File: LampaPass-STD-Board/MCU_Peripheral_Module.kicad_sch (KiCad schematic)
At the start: 0 parts

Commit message: Added draw schematics of MCU and peripheral. Added datasheets of ESP32 dev module and voltage supervisor.
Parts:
- added BZ1: Buzzer, symbol Device:Buzzer
- added C5, C6: 0.1u/6.3V, symbol Device:C_Small
- added C7: 10u/6.3V, symbol Device:C_Small
- added J1, J7: Conn_01x04_Pin, symbol Connector:Conn_01x04_Pin
- added J10: Screw_Terminal_01x05, symbol Connector:Screw_Terminal_01x05
- added J3: Conn_01x02_Pin, symbol Connector:Conn_01x02_Pin
- added J4: Conn_01x08_Socket, symbol Connector:Conn_01x08_Socket
- added J5: Conn_01x03_Socket, symbol Connector:Conn_01x03_Socket
- added J6: Conn_01x06_Pin, symbol Connector:Conn_01x06_Pin
- added J8: Conn_01x04_Socket, symbol Connector:Conn_01x04_Socket
- added Q3, Q4: NMOS, symbol Simulation_SPICE:NMOS
- added R10: 820, symbol Device:R
- added R11, R13, R8, R9: 160, symbol Device:R
- added R12: 1k, symbol Device:R
- added R14, R15, R7: 10k, symbol Device:R
- added U3: ESP32-WROOM-32, RF_Module:ESP32-WROOM-32, symbol RF_Module:ESP32-WROOM-32
- added U5: BD48KxxG, Package_TO_SOT_SMD:SOT-23, symbol Power_Management:BD48KxxG
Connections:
- new net: Q4.2 (G), R13.2
- new net: C5.1, R7.2, U3.3 (EN), U5.2 (VOUT)
- new net: J10.5 (Pin_5), Q4.1 (D)
- new net: BZ1.2 (+), Q3.1 (D), R12.1
- new net: Q3.2 (G), R11.1
- new net: J3.2 (Pin_2), U3.25 (IO0)
- new net +3.3V: BZ1.1 (-), C6.2, C7.2, J1.1 (Pin_1), J10.2 (Pin_2), J4.5 (Pin_5), J5.1 (Pin_1), J6.6 (Pin_6), J7.1 (Pin_1), J8.3 (Pin_3), R12.2, R7.1, U3.2 (VDD), U5.3 (VDD)
- new net +9V: J10.4 (Pin_4)
- new net BLUE: J8.2 (Pin_2), R9.1
- new net BLUE_LED: R9.2, U3.13 (IO14)
- new net BUZZ: R11.2, U3.16 (IO13)
- new net Batt_V_analog: U3.6 (IO34)
- new net Charge_EN: U3.11 (IO26)
- new net Charge_info: U3.10 (IO25)
- new net GND: C5.2, C6.1, C7.1, J1.4 (Pin_4), J3.1 (Pin_1), J4.6 (Pin_6), J5.3 (Pin_3), J6.1 (Pin_1), J7.4 (Pin_4), Q3.3 (S), Q4.3 (S), R14.1, R15.1, U3.1 (GND), U3.15 (GND), U3.38 (GND), U3.39 (GND), U5.1 (GND)
- new net GREEN: J8.1 (Pin_1), R8.1
- new net GREEN_LED: R8.2, U3.14 (IO12)
- new net MISO1: J4.2 (Pin_2), J6.3 (Pin_3), U3.30 (IO18)
- new net MOSI1: J4.3 (Pin_3), J6.4 (Pin_4), U3.31 (IO19)
- new net NC_Solenoid: J10.3 (Pin_3), R14.2, U3.36 (IO22)
- new net NO_Solenoid: J10.1 (Pin_1), R15.2, U3.37 (IO23)
- new net PIR_data: J5.2 (Pin_2), U3.7 (IO35)
- new net RED: J8.4 (Pin_4), R10.1
- new net RED_LED: R10.2, U3.12 (IO27)
- new net SLK1: J4.1 (Pin_1), J6.2 (Pin_2), U3.29 (IO5)
- new net SS_Out_Spi: J6.5 (Pin_5), U3.24 (IO2)
- new net SS_pn532: J4.4 (Pin_4), U3.23 (IO15)
- new net Solenoid: R13.1, U3.26 (IO4)
- new net UART0_ESP32_RX: J1.3 (Pin_3), U3.34 (RXD0/IO3)
- new net UART0_ESP32_TX: J1.2 (Pin_2), U3.35 (TXD0/IO1)
- new net UART2_ESP32_RX: J7.3 (Pin_3), U3.27 (IO16)
- new net UART2_ESP32_TX: J7.2 (Pin_2), U3.28 (IO17)
- no-connect marks 0 -> 8
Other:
- note added: "BOOT OPTION"
- note added: "CONN PIR AM312"
- note added: "CONN pn532"
- note added: "RGB LED CONN"
- note added: "SPI CONN"
- note added: "Solenoid CONN"
- note added: "UART0 DOWNLOAD"
- note added: "UART2 CONN"
- note added: "Worning Can be placed upside down!"

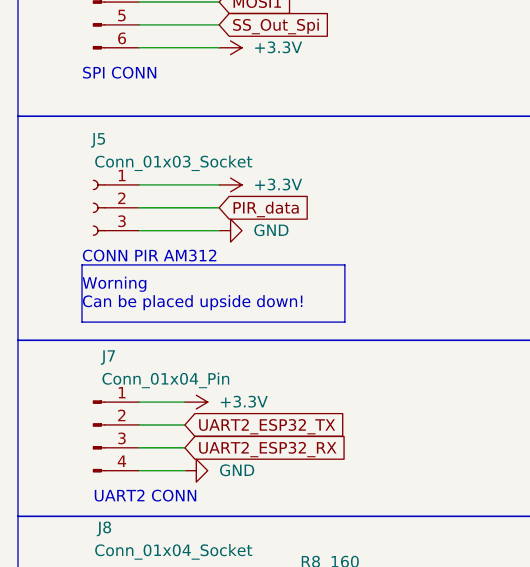
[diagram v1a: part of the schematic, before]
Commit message: Added Battery Backup Power Module. Added Power Mangement empty schematic.
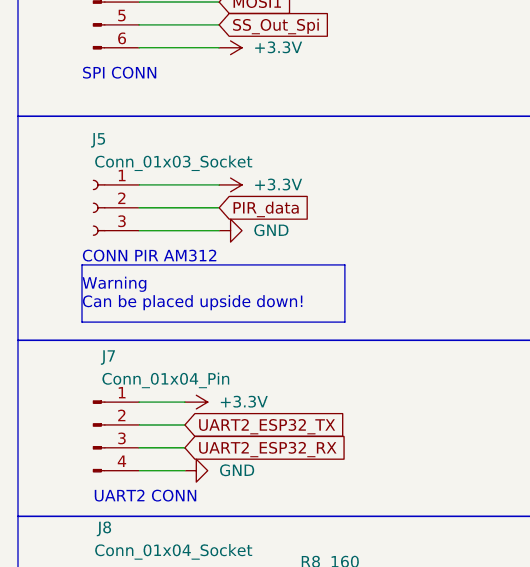
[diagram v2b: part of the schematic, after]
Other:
- note added: "Warning Can be placed upside down!"
- note removed: "Worning Can be placed upside down!"
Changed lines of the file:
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@@
     (effects (font (size 1.27 1.27)) (justify left bottom))
   )
-  (text "Worning \nCan be placed upside down!" (at 19.05 92.71 0)
+  (text "Warning \nCan be placed upside down!" (at 19.05 92.71 0)
     (effects (font (size 1.27 1.27)) (justify left bottom))
   )

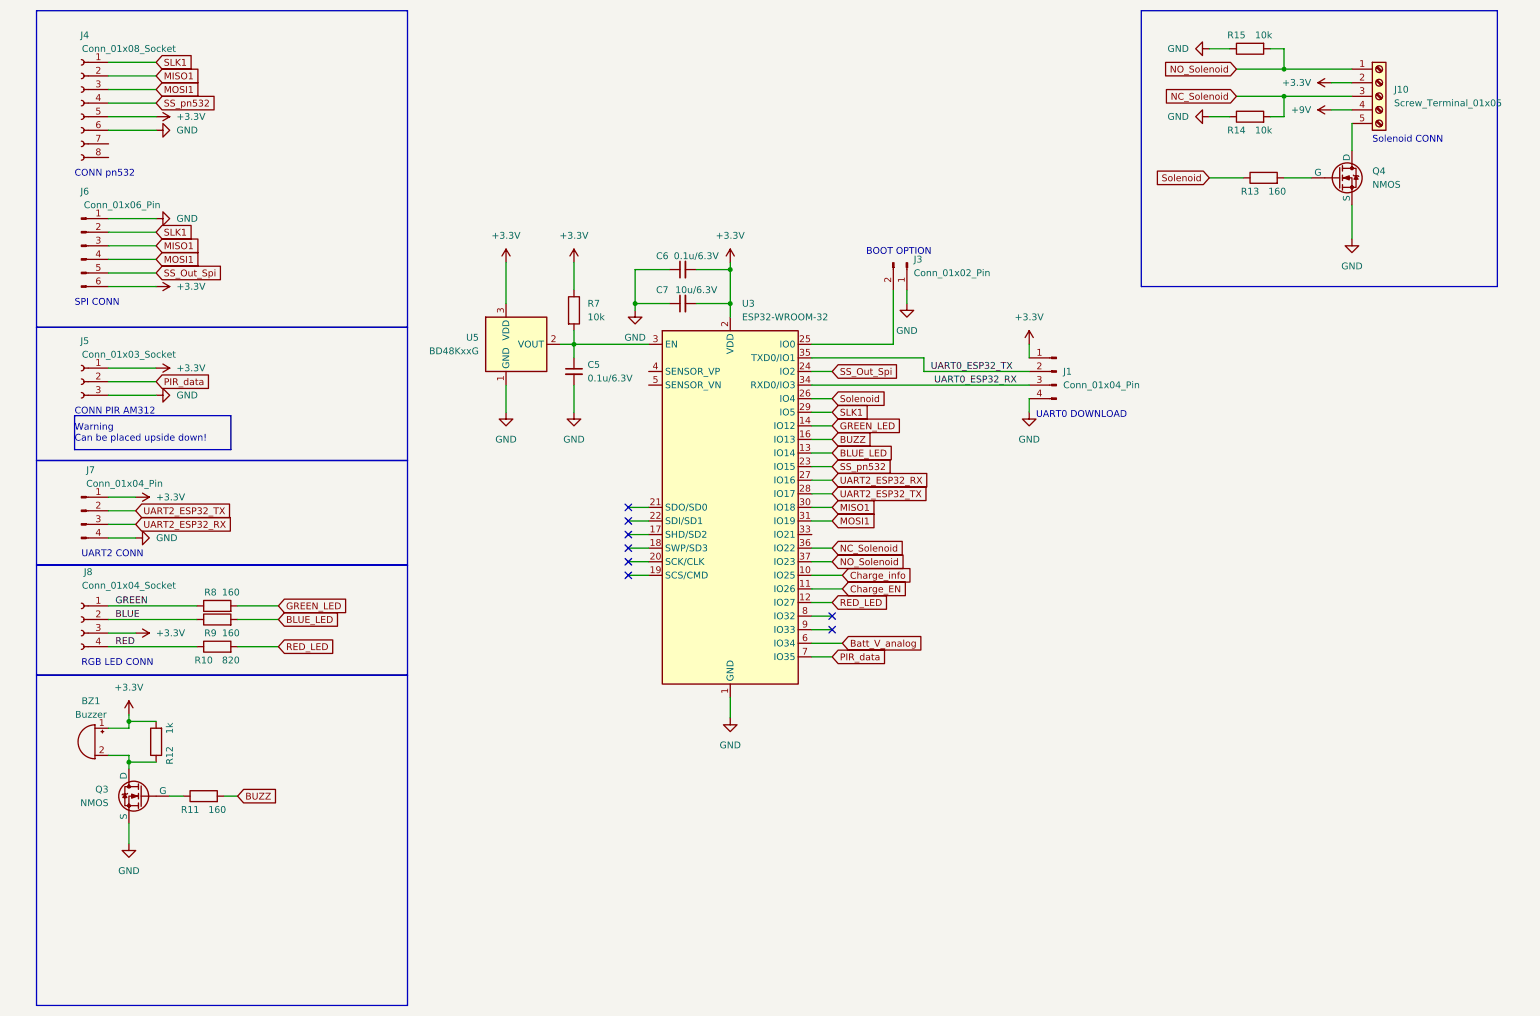
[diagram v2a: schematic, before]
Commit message: Selected connectors and transistors, added footprints for them.
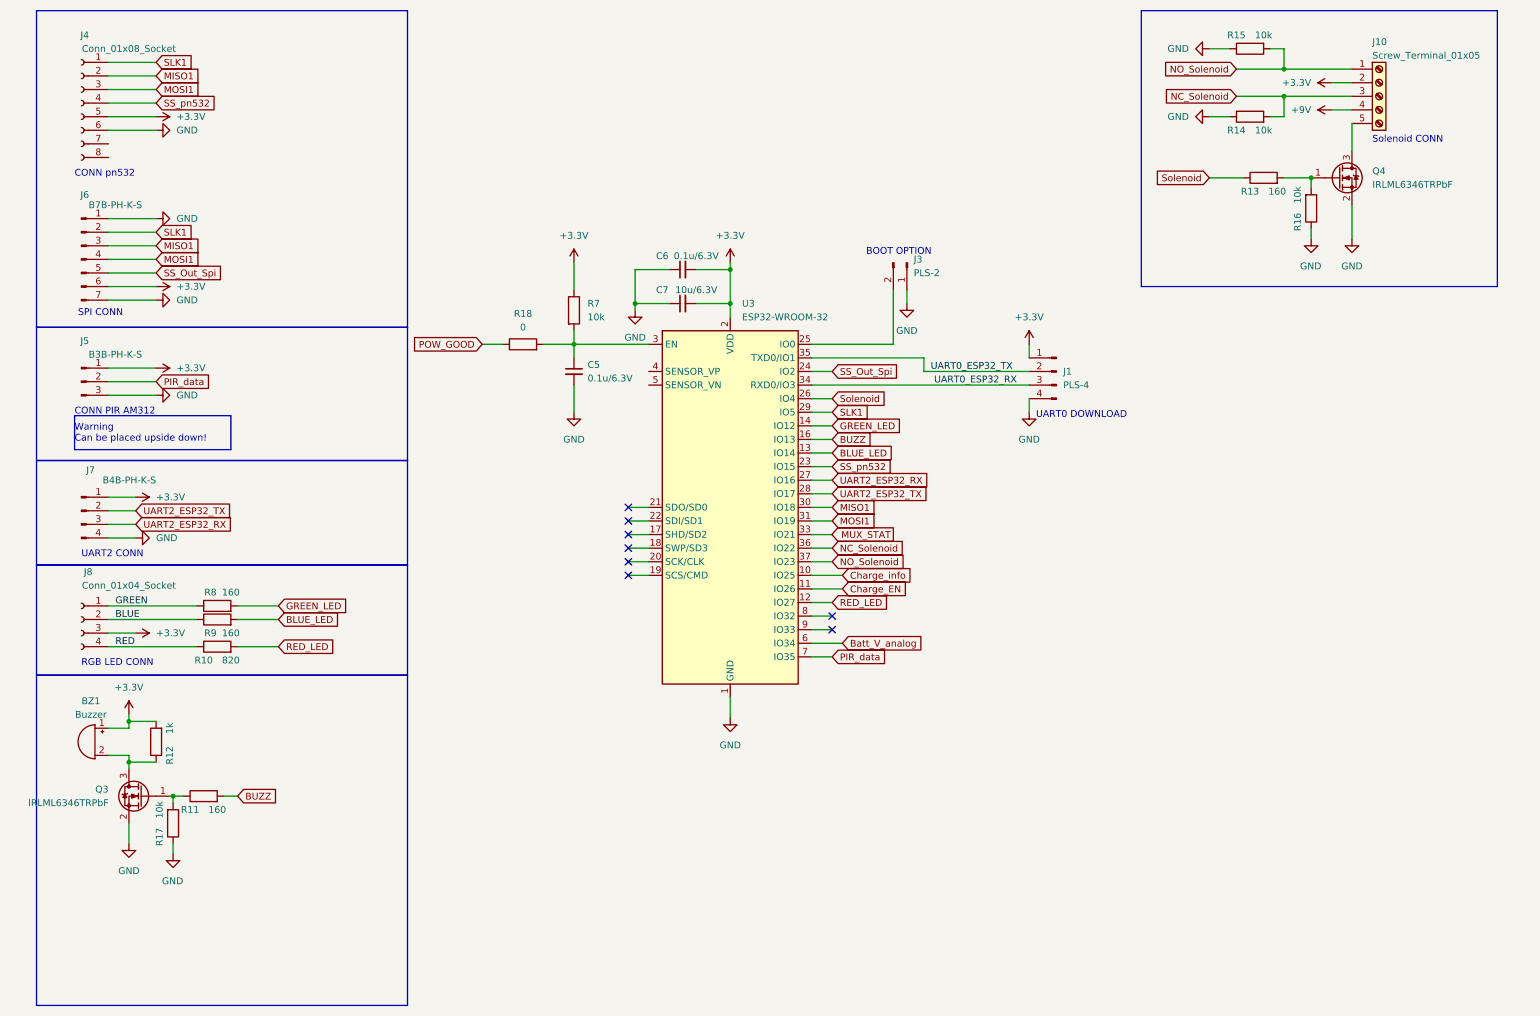
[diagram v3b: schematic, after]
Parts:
- removed J6: Conn_01x06_Pin, symbol Connector:Conn_01x06_Pin
- removed Q4: NMOS, symbol Simulation_SPICE:NMOS
- removed U5: BD48KxxG, Package_TO_SOT_SMD:SOT-23, symbol Power_Management:BD48KxxG
- added J6: B7B-PH-K-S, Connector_JST:JST_PH_B7B-PH-K_1x07_P2.00mm_Vertical, symbol Connector:Conn_01x07_Pin
- added Q4: IRLML6346TRPbF, Package_TO_SOT_SMD:SOT-23, symbol Device:Q_NMOS_GSD
- added R16, R17: 10k, symbol Device:R
- added R18: 0, symbol Device:R
- J1: value Conn_01x04_Pin -> PLS-4; footprint (none) -> Connector_PinHeader_2.54mm:PinHeader_1x04_P2.54mm_Vertical; PartNamber (none) -> PLS-4
- J10: footprint (none) -> TerminalBlock_Phoenix:TerminalBlock_Phoenix_MKDS-1,5-5_1x05_P5.00mm_Horizontal; PartNamber (none) -> 1935190
- J3: value Conn_01x02_Pin -> PLS-2; footprint (none) -> Connector_PinHeader_2.54mm:PinHeader_1x02_P2.54mm_Vertical; PartNamber (none) -> PLS-2
- J4: footprint (none) -> Connector_PinHeader_2.54mm:PinHeader_1x08_P2.54mm_Vertical; PartNamber (none) -> PLS-8
- J5: value Conn_01x03_Socket -> B3B-PH-K-S; footprint (none) -> Connector_JST:JST_PH_B3B-PH-K_1x03_P2.00mm_Vertical; symbol Connector:Conn_01x03_Socket -> Connector:Conn_01x03_Pin; PartNamber (none) -> B3B-PH-K-S
- J7: value Conn_01x04_Pin -> B4B-PH-K-S; footprint (none) -> Connector_JST:JST_PH_B4B-PH-K_1x04_P2.00mm_Vertical
- J8: footprint (none) -> Connector_PinHeader_2.54mm:PinHeader_1x04_P2.54mm_Vertical
- Q3: value NMOS -> IRLML6346TRPbF; footprint (none) -> Package_TO_SOT_SMD:SOT-23; symbol Simulation_SPICE:NMOS -> Device:Q_NMOS_GSD; PartNamber (none) -> IRLML6346TRPbF
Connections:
- net +3.3V: now also J6.6 (Pin_6)
- net GND: now also Q3.2 (S), J6.1 (Pin_1), J6.7 (Pin_7), Q4.2 (S), R16.1, R17.1; no longer Q3.3 (S)
- net MISO1: now also J6.3 (Pin_3)
- net MOSI1: now also J6.4 (Pin_4)
- net SLK1: now also J6.2 (Pin_2)
- net SS_Out_Spi: now also J6.5 (Pin_5)
- net at R13.2: now also Q4.1 (G), R16.2
- net at C5.1, R7.2, U3.3 (EN): now also R18.2
- net at J10.5 (Pin_5): now also Q4.3 (D)
- net at BZ1.2 (+), R12.1: now also Q3.3 (D); no longer Q3.1 (D)
- net at R11.1: now also Q3.1 (G), R17.2; no longer Q3.2 (G)
- new net POW_GOOD: R18.1
